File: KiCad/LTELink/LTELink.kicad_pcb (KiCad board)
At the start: 4 copper layers, 93.3 x 58.9 mm, 102 parts, among them IC1 RTL8305NB-VC-CG, J1 DF40HC(3.0)-100DS-0.4V(51), J13 Conn_01x04, J14 Conn_01x04, J15 Conn_01x04, J19 Conn_01x04, J2 DF40HC(3.0)-100DS-0.4V(51), J21 Conn_01x04, J22 Conn_01x04, J23 Conn_01x04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

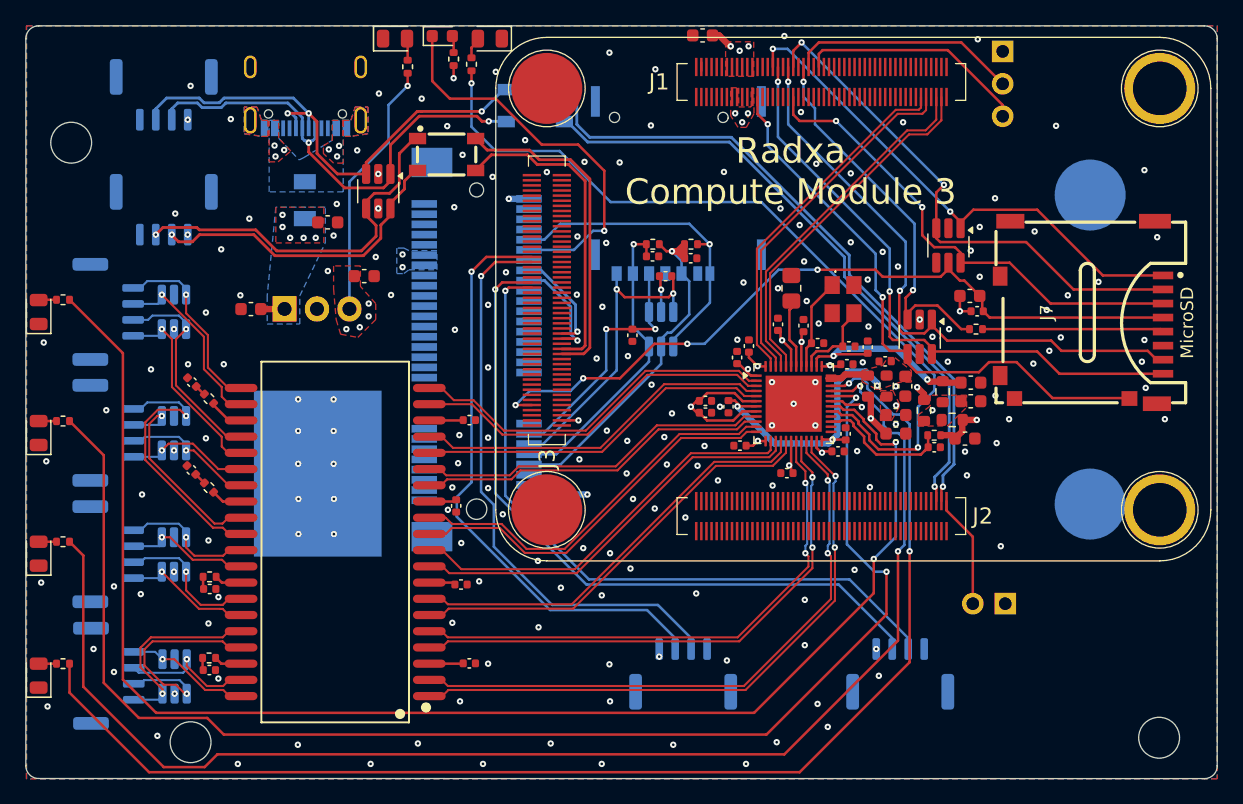
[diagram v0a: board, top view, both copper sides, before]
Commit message: Moved LEDs to other side of the board, which means they mustbe assembled by hand. Added UART 5 test points.
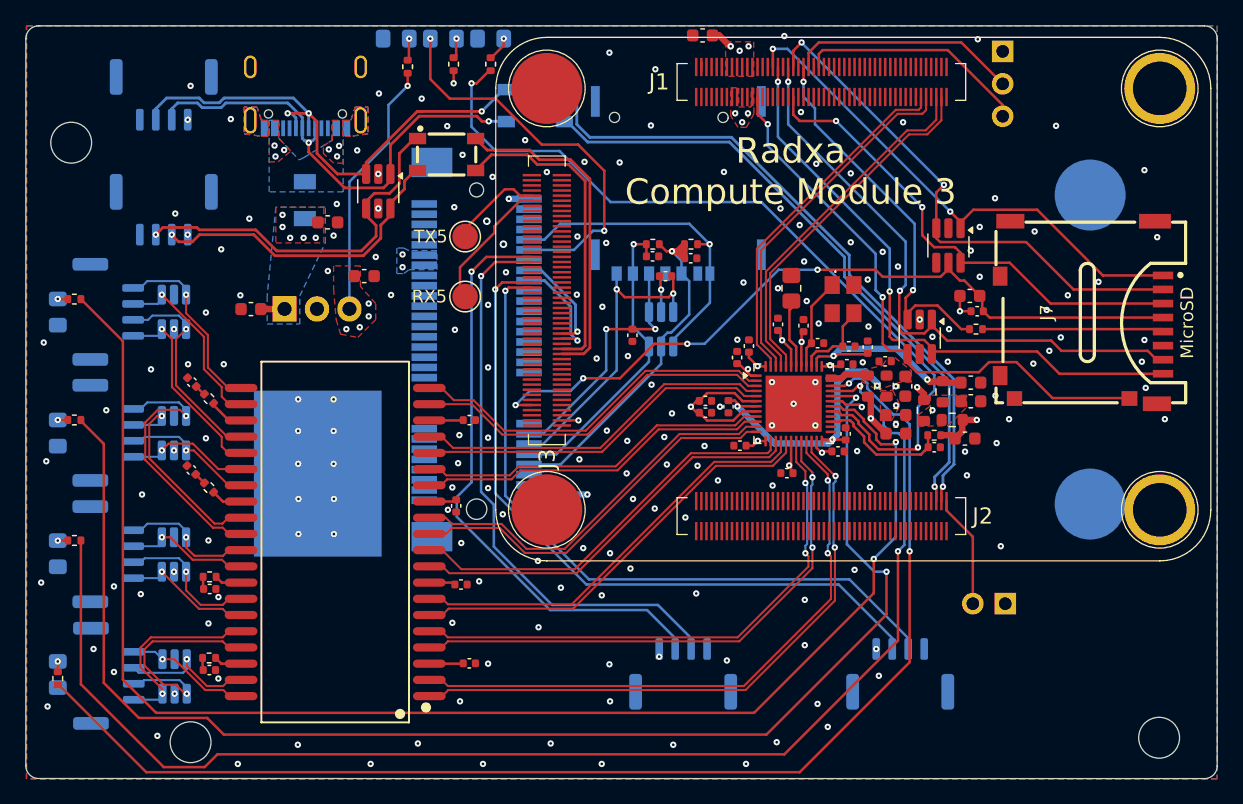
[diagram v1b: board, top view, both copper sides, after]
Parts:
- added RX5: TestPoint, TestPoint:TestPoint_Pad_D2.0mm, F.Cu at (182.1, 77.8)
- added TX5: TestPoint, TestPoint:TestPoint_Pad_D2.0mm, F.Cu at (182.1, 73.1)
- D10: footprint LED_SMD:LED_0603_1608Metric -> LED_SMD:LED_0805_2012Metric_Pad1.15x1.40mm_HandSolder; moved to B.Cu
- D11, D12, D13, D14, D15, D9: footprint LED_SMD:LED_0805_2012Metric -> LED_SMD:LED_0805_2012Metric_Pad1.15x1.40mm_HandSolder; moved to B.Cu
- moved D15 1.50 mm to (150.2, 107.4)
- moved R7 1.50 mm to (184.1, 59.6)
- moved D12 1.50 mm to (150.2, 79.0)
- moved D13 1.50 mm to (150.2, 88.5)
- moved D14 1.50 mm to (150.2, 97.9)
- moved R24 1.22 mm to (150.2, 107.7), turned to 90 degrees
- moved R22 0.90 mm to (151.5, 96.9)
- moved R10 0.89 mm to (151.5, 87.5)
- moved R9 0.89 mm to (151.5, 78.0)
- moved R16 0.40 mm to (181.2, 59.6)
- moved D10 0.22 mm to (180.4, 57.6)
- moved D9 0.09 mm to (176.7, 57.6)
- moved D11 0.06 mm to (184.1, 57.6), turned to 0 degrees
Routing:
- net /Compute Module/UART5_RX: track 0.00 -> 10.5 mm
- net /Compute Module/UART5_TX: track 0.00 -> 7.31 mm
- net /Ethernet/P4LED: track 101.0 -> 99.9 mm
- net /Ethernet/P0LED: track 63.4 -> 64.3 mm
- net Net-(D12-A): track 1.41 -> 0.80 mm, vias 0 -> 1
- net Net-(D13-A): track 1.41 -> 0.79 mm, vias 0 -> 1
- net Net-(D14-A): track 1.41 -> 0.80 mm, vias 0 -> 1
- net Net-(D15-A): track 1.41 -> 0.81 mm, vias 0 -> 1
- net Net-(D11-A): track 1.70 -> 1.95 mm, vias 0 -> 1
- net Net-(D10-A): track 1.33 -> 1.58 mm, vias 0 -> 1
- net Net-(D10-K): track 31.1 -> 31.0 mm, vias 1 -> 2
- net Net-(D9-A): track 1.72 -> 1.74 mm, vias 0 -> 1
- net GND: vias 186 -> 187
